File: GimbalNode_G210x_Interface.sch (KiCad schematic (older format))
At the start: 6 parts, among them P1 CONN_01X08_2MNT, P2 CONN_01X08_2MNT, U1 74HCT157, U2 74HCT157

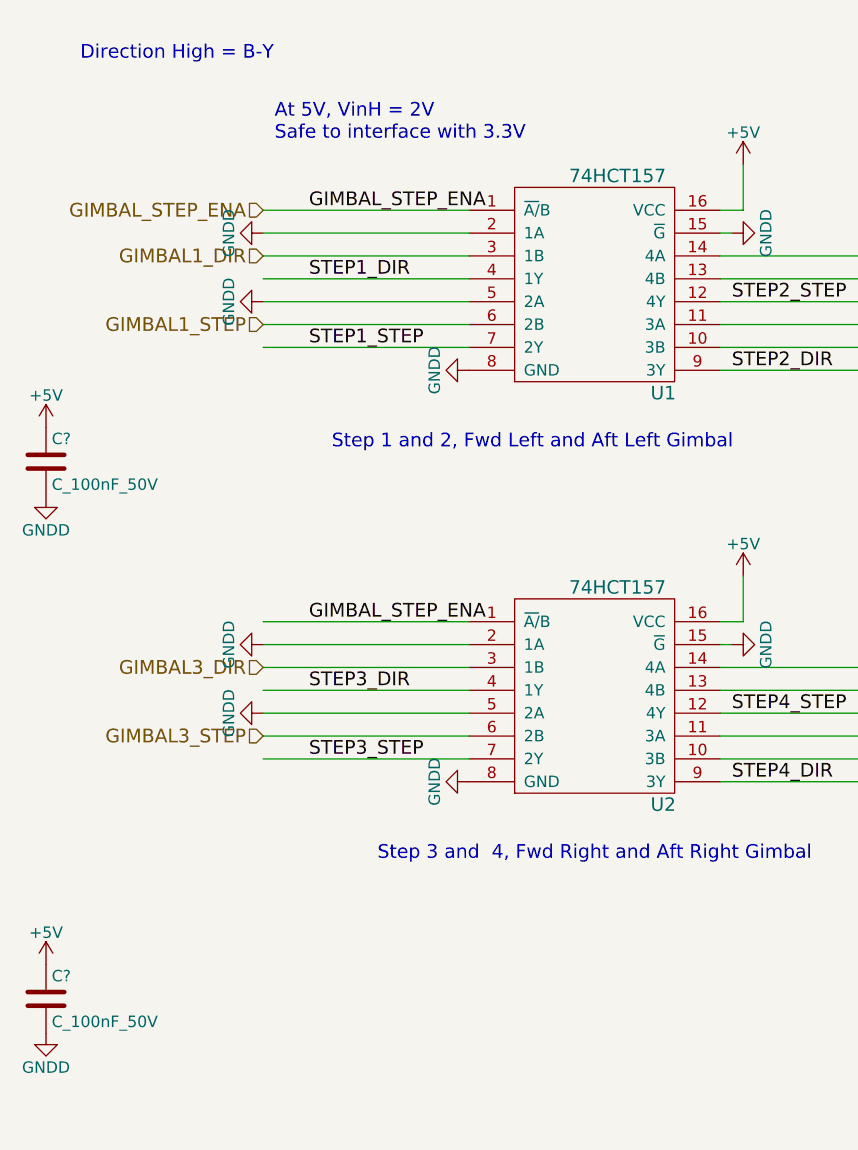
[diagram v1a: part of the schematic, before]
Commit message: Fixup 5V to 3V connections
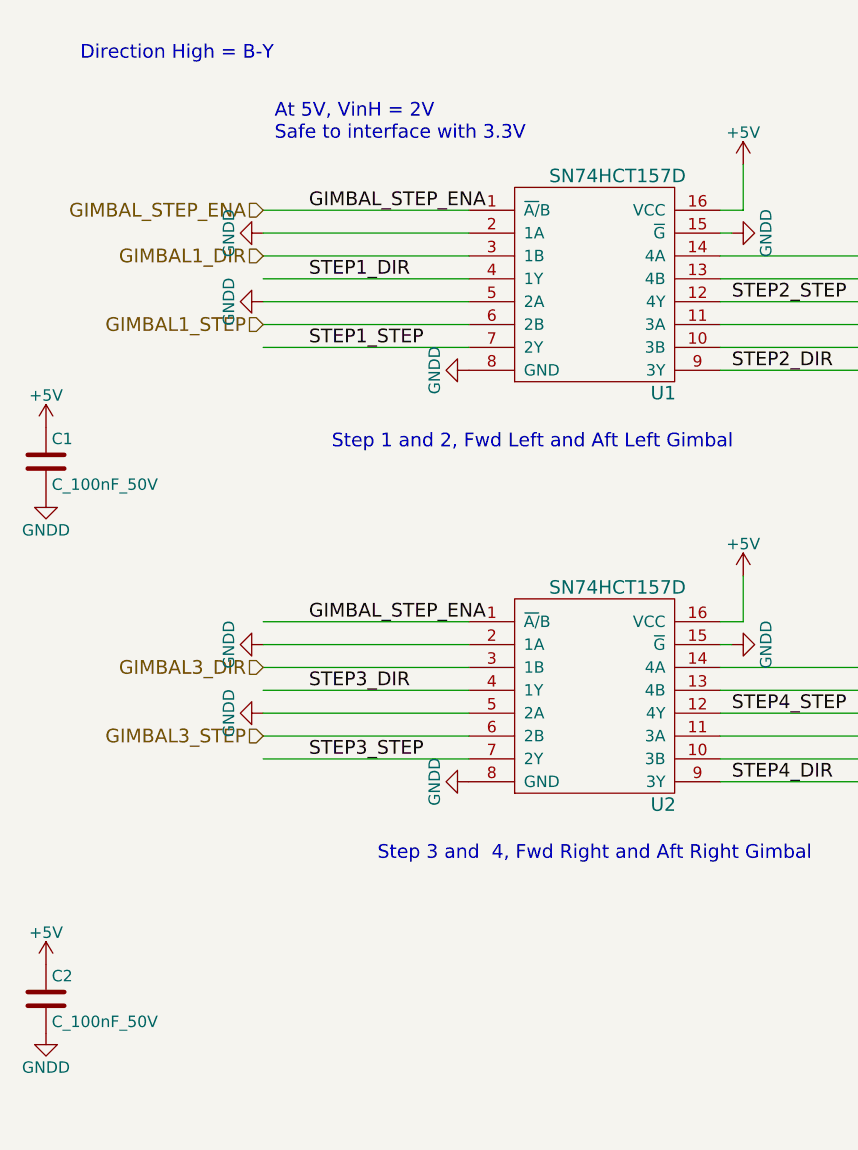
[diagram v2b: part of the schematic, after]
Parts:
- removed U1, U2: 74HCT157, symbol 74HCT157
- added U1, U2: SN74HCT157D, RLOOP_FOOTPRINTS:rLoop_SOIC_16, symbol SN74HCT157D
- gave numbers to parts that had none: 2
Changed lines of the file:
@@
 	12500 3200 11650 3200
 $Comp
-L GNDD #PWR05
+L GNDD #PWR25
 U 1 1 5757EB8B
 P 12500 3000
-F 0 "#PWR05" H 12500 2750 50  0001 C CNN
+F 0 "#PWR25" H 12500 2750 50  0001 C CNN
 F 1 "GNDD" H 12500 2850 50  0000 C CNN
 F 2 "" H 12500 3000 50  0000 C CNN
@@
 $EndComp
 $Comp
-L GNDD #PWR06
+L GNDD #PWR26
 U 1 1 5757EB8C
 P 12500 3300
-F 0 "#PWR06" H 12500 3050 50  0001 C CNN
+F 0 "#PWR26" H 12500 3050 50  0001 C CNN
 F 1 "GNDD" H 12500 3150 50  0000 C CNN
 F 2 "" H 12500 3300 50  0000 C CNN
@@
 	12450 5100 11600 5100
 $Comp
-L GNDD #PWR07
+L GNDD #PWR23
 U 1 1 5757EB8E
 P 12450 4900
-F 0 "#PWR07" H 12450 4650 50  0001 C CNN
+F 0 "#PWR23" H 12450 4650 50  0001 C CNN
 F 1 "GNDD" H 12450 4750 50  0000 C CNN
 F 2 "" H 12450 4900 50  0000 C CNN
@@
 $EndComp
 $Comp
-L GNDD #PWR08
+L GNDD #PWR24
 U 1 1 5757EB8F
 P 12450 5200
-F 0 "#PWR08" H 12450 4950 50  0001 C CNN
+F 0 "#PWR24" H 12450 4950 50  0001 C CNN
 F 1 "GNDD" H 12450 5050 50  0000 C CNN
 F 2 "" H 12450 5200 50  0000 C CNN
@@
 Text Notes 12000 10500 0    60   ~ 0
 Original Author: SafetyLok
-$Comp
-L 74HCT157 U1
-U 1 1 5757EB93
-P 6250 4050
-F 0 "U1" H 6900 4000 59  0000 C CNN
-F 1 "74HCT157" H 6700 4950 59  0000 C CNN
-F 2 "" H 6250 4050 197 0000 C CNN
-F 3 "" H 6250 4050 197 0000 C CNN
-	1    6250 4050
-	1    0    0    -1
-$EndComp
 Wire Wire Line
 	7150 3300 7250 3300
@@
 	6050 3900 5150 3900
 $Comp
-L GNDD #PWR09
+L GNDD #PWR15
 U 1 1 5757EB94
 P 7200 3400
-F 0 "#PWR09" H 7200 3150 50  0001 C CNN
+F 0 "#PWR15" H 7200 3150 50  0001 C CNN
 F 1 "GNDD" H 7200 3250 50  0000 C CNN
 F 2 "" H 7200 3400 50  0000 C CNN
@@
 	7150 3400 7200 3400
 $Comp
-L GNDD #PWR010
+L GNDD #PWR13
 U 1 1 5757EB95
 P 6050 4000
-F 0 "#PWR010" H 6050 3750 50  0001 C CNN
+F 0 "#PWR13" H 6050 3750 50  0001 C CNN
 F 1 "GNDD" H 6050 3850 50  0000 C CNN
 F 2 "" H 6050 4000 50  0000 C CNN
@@
 GIMBAL_STEP_ENA
 $Comp
-L +5V #PWR011
+L +5V #PWR17
 U 1 1 5757EB96
 P 7250 3100
-F 0 "#PWR011" H 7250 2950 50  0001 C CNN
+F 0 "#PWR17" H 7250 2950 50  0001 C CNN
 F 1 "+5V" H 7250 3240 50  0000 C CNN
 F 2 "" H 7250 3100 50  0000 C CNN
@@
 	1    0    0    -1
 $EndComp
-$Comp
-L 74HCT157 U2
-U 1 1 5757EB97
-P 6250 5850
-F 0 "U2" H 6900 5800 59  0000 C CNN
-F 1 "74HCT157" H 6700 6750 59  0000 C CNN
-F 2 "" H 6250 5850 197 0000 C CNN
-F 3 "" H 6250 5850 197 0000 C CNN
-	1    6250 5850
-	1    0    0    -1
-$EndComp
 Wire Wire Line
 	7150 5100 7250 5100
@@
 	6050 5700 5150 5700
 $Comp
-L GNDD #PWR012
+L GNDD #PWR16
 U 1 1 5757EB98
 P 7200 5200
-F 0 "#PWR012" H 7200 4950 50  0001 C CNN
+F 0 "#PWR16" H 7200 4950 50  0001 C CNN
 F 1 "GNDD" H 7200 5050 50  0000 C CNN
 F 2 "" H 7200 5200 50  0000 C CNN
@@
 GIMBAL_STEP_ENA
 $Comp
-L +5V #PWR013
+L +5V #PWR18
 U 1 1 5757EB9A
 P 7250 4900
-F 0 "#PWR013" H 7250 4750 50  0001 C CNN
+F 0 "#PWR18" H 7250 4750 50  0001 C CNN
 F 1 "+5V" H 7250 5040 50  0000 C CNN
 F 2 "" H 7250 4900 50  0000 C CNN
@@
 STEP4_STEP
 $Comp
-L GNDD #PWR014
+L GNDD #PWR9
 U 1 1 5757F02C
 P 5150 3400
-F 0 "#PWR014" H 5150 3150 50  0001 C CNN
+F 0 "#PWR9" H 5150 3150 50  0001 C CNN
 F 1 "GNDD" H 5150 3250 50  0000 C CNN
 F 2 "" H 5150 3400 50  0000 C CNN
@@
 $EndComp
 $Comp
-L GNDD #PWR015
+L GNDD #PWR10
 U 1 1 5757F037
 P 5150 3700
-F 0 "#PWR015" H 5150 3450 50  0001 C CNN
+F 0 "#PWR10" H 5150 3450 50  0001 C CNN
 F 1 "GNDD" H 5150 3550 50  0000 C CNN
 F 2 "" H 5150 3700 50  0000 C CNN
@@
 $EndComp
 $Comp
-L GNDD #PWR016
+L GNDD #PWR11
 U 1 1 5757F042
 P 5150 5200
-F 0 "#PWR016" H 5150 4950 50  0001 C CNN
+F 0 "#PWR11" H 5150 4950 50  0001 C CNN
 F 1 "GNDD" H 5150 5050 50  0000 C CNN
 F 2 "" H 5150 5200 50  0000 C CNN
@@
 $EndComp
 $Comp
-L GNDD #PWR017
+L GNDD #PWR12
 U 1 1 5757F04D
 P 5150 5500
-F 0 "#PWR017" H 5150 5250 50  0001 C CNN
+F 0 "#PWR12" H 5150 5250 50  0001 C CNN
 F 1 "GNDD" H 5150 5350 50  0000 C CNN
 F 2 "" H 5150 5500 50  0000 C CNN
@@
 $EndComp
 $Comp
-L GNDD #PWR018
+L GNDD #PWR19
 U 1 1 5757F058
 P 7950 3500
-F 0 "#PWR018" H 7950 3250 50  0001 C CNN
+F 0 "#PWR19" H 7950 3250 50  0001 C CNN
 F 1 "GNDD" H 7950 3350 50  0000 C CNN
 F 2 "" H 7950 3500 50  0000 C CNN
@@
 $EndComp
 $Comp
-L GNDD #PWR019
+L GNDD #PWR20
 U 1 1 5757F063
 P 7950 3800
-F 0 "#PWR019" H 7950 3550 50  0001 C CNN
+F 0 "#PWR20" H 7950 3550 50  0001 C CNN
 F 1 "GNDD" H 7950 3650 50  0000 C CNN
 F 2 "" H 7950 3800 50  0000 C CNN
@@
 $EndComp
 $Comp
-L GNDD #PWR020
+L GNDD #PWR21
 U 1 1 5757F078
 P 7950 5300
-F 0 "#PWR020" H 7950 5050 50  0001 C CNN
+F 0 "#PWR21" H 7950 5050 50  0001 C CNN
 F 1 "GNDD" H 7950 5150 50  0000 C CNN
 F 2 "" H 7950 5300 50  0000 C CNN
@@
 $EndComp
 $Comp
-L GNDD #PWR021
+L GNDD #PWR22
 U 1 1 5757F083
 P 7950 5600
-F 0 "#PWR021" H 7950 5350 50  0001 C CNN
+F 0 "#PWR22" H 7950 5350 50  0001 C CNN
 F 1 "GNDD" H 7950 5450 50  0000 C CNN
 F 2 "" H 7950 5600 50  0000 C CNN
@@
 $EndComp
 $Comp
-L GNDD #PWR022
+L GNDD #PWR14
 U 1 1 5758A913
 P 6050 5800
-F 0 "#PWR022" H 6050 5550 50  0001 C CNN
+F 0 "#PWR14" H 6050 5550 50  0001 C CNN
 F 1 "GNDD" H 6050 5650 50  0000 C CNN
 F 2 "" H 6050 5800 50  0000 C CNN
@@
 $EndComp
 $Comp
-L GNDD #PWR023
+L GNDD #PWR6
 U 1 1 5758AA2C
 P 4200 4550
-F 0 "#PWR023" H 4200 4300 50  0001 C CNN
+F 0 "#PWR6" H 4200 4300 50  0001 C CNN
 F 1 "GNDD" H 4200 4400 50  0000 C CNN
 F 2 "" H 4200 4550 50  0000 C CNN
@@
 $EndComp
 $Comp
-L +5V #PWR024
+L +5V #PWR5
 U 1 1 5758AA38
 P 4200 4250
-F 0 "#PWR024" H 4200 4100 50  0001 C CNN
+F 0 "#PWR5" H 4200 4100 50  0001 C CNN
 F 1 "+5V" H 4200 4390 50  0000 C CNN
 F 2 "" H 4200 4250 50  0000 C CNN
@@
 $EndComp
 $Comp
-L GNDD #PWR025
+L GNDD #PWR8
 U 1 1 5758AAB6
 P 4200 6900
-F 0 "#PWR025" H 4200 6650 50  0001 C CNN
+F 0 "#PWR8" H 4200 6650 50  0001 C CNN
 F 1 "GNDD" H 4200 6750 50  0000 C CNN
 F 2 "" H 4200 6900 50  0000 C CNN
@@
 $EndComp
 $Comp
-L +5V #PWR026
+L +5V #PWR7
 U 1 1 5758AAC2
 P 4200 6600
-F 0 "#PWR026" H 4200 6450 50  0001 C CNN
+F 0 "#PWR7" H 4200 6450 50  0001 C CNN
 F 1 "+5V" H 4200 6740 50  0000 C CNN
 F 2 "" H 4200 6600 50  0000 C CNN
@@
 $EndComp
 $Comp
-L C_100nF_50V C?
+L C_100nF_50V C1
 U 1 1 5758DE9D
 P 4200 4400
-F 0 "C?" H 4225 4500 50  0000 L CNN
+F 0 "C1" H 4225 4500 50  0000 L CNN
 F 1 "C_100nF_50V" H 4225 4300 50  0000 L CNN
 F 2 "RLOOP_FOOTPRINTS:rLoop_C_0603" H 4238 4250 50  0001 C CNN
@@
 $EndComp
 $Comp
-L C_100nF_50V C?
+L C_100nF_50V C2
 U 1 1 5758DF8E
 P 4200 6750
-F 0 "C?" H 4225 6850 50  0000 L CNN
+F 0 "C2" H 4225 6850 50  0000 L CNN
 F 1 "C_100nF_50V" H 4225 6650 50  0000 L CNN
 F 2 "RLOOP_FOOTPRINTS:rLoop_C_0603" H 4238 6600 50  0001 C CNN
@@
 	1    0    0    -1
 $EndComp
+$Comp
+L SN74HCT157D U1
+U 1 1 575AB2B3
+P 6250 4050
+F 0 "U1" H 6900 4000 59  0000 C CNN
+F 1 "SN74HCT157D" H 6700 4950 59  0000 C CNN
+F 2 "RLOOP_FOOTPRINTS:rLoop_SOIC_16" H 6800 3900 197 0001 C CNN
+F 3 "" H 6250 4050 197 0000 C CNN
+	1    6250 4050
+	1    0    0    -1
+$EndComp
+$Comp
+L SN74HCT157D U2
+U 1 1 575AB35E
+P 6250 5850
+F 0 "U2" H 6900 5800 59  0000 C CNN
+F 1 "SN74HCT157D" H 6700 6750 59  0000 C CNN
+F 2 "RLOOP_FOOTPRINTS:rLoop_SOIC_16" H 6800 5700 197 0001 C CNN
+F 3 "" H 6250 5850 197 0000 C CNN
+	1    6250 5850
+	1    0    0    -1
+$EndComp
